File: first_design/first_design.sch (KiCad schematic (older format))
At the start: 57 parts

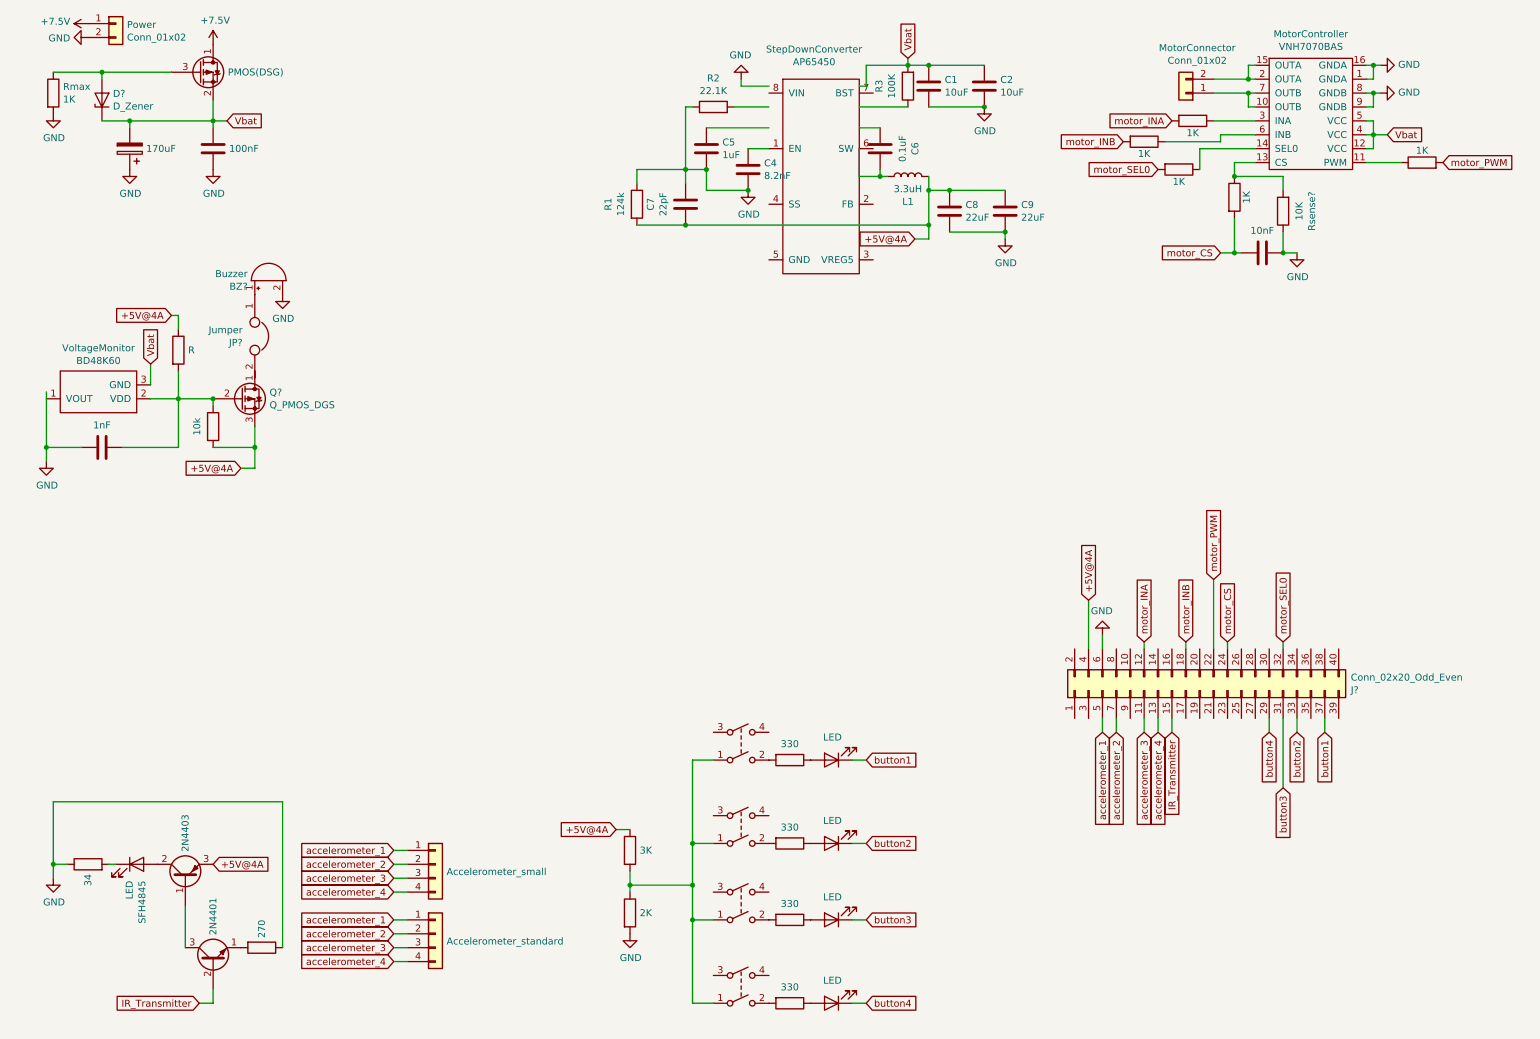
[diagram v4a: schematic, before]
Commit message: ldo added
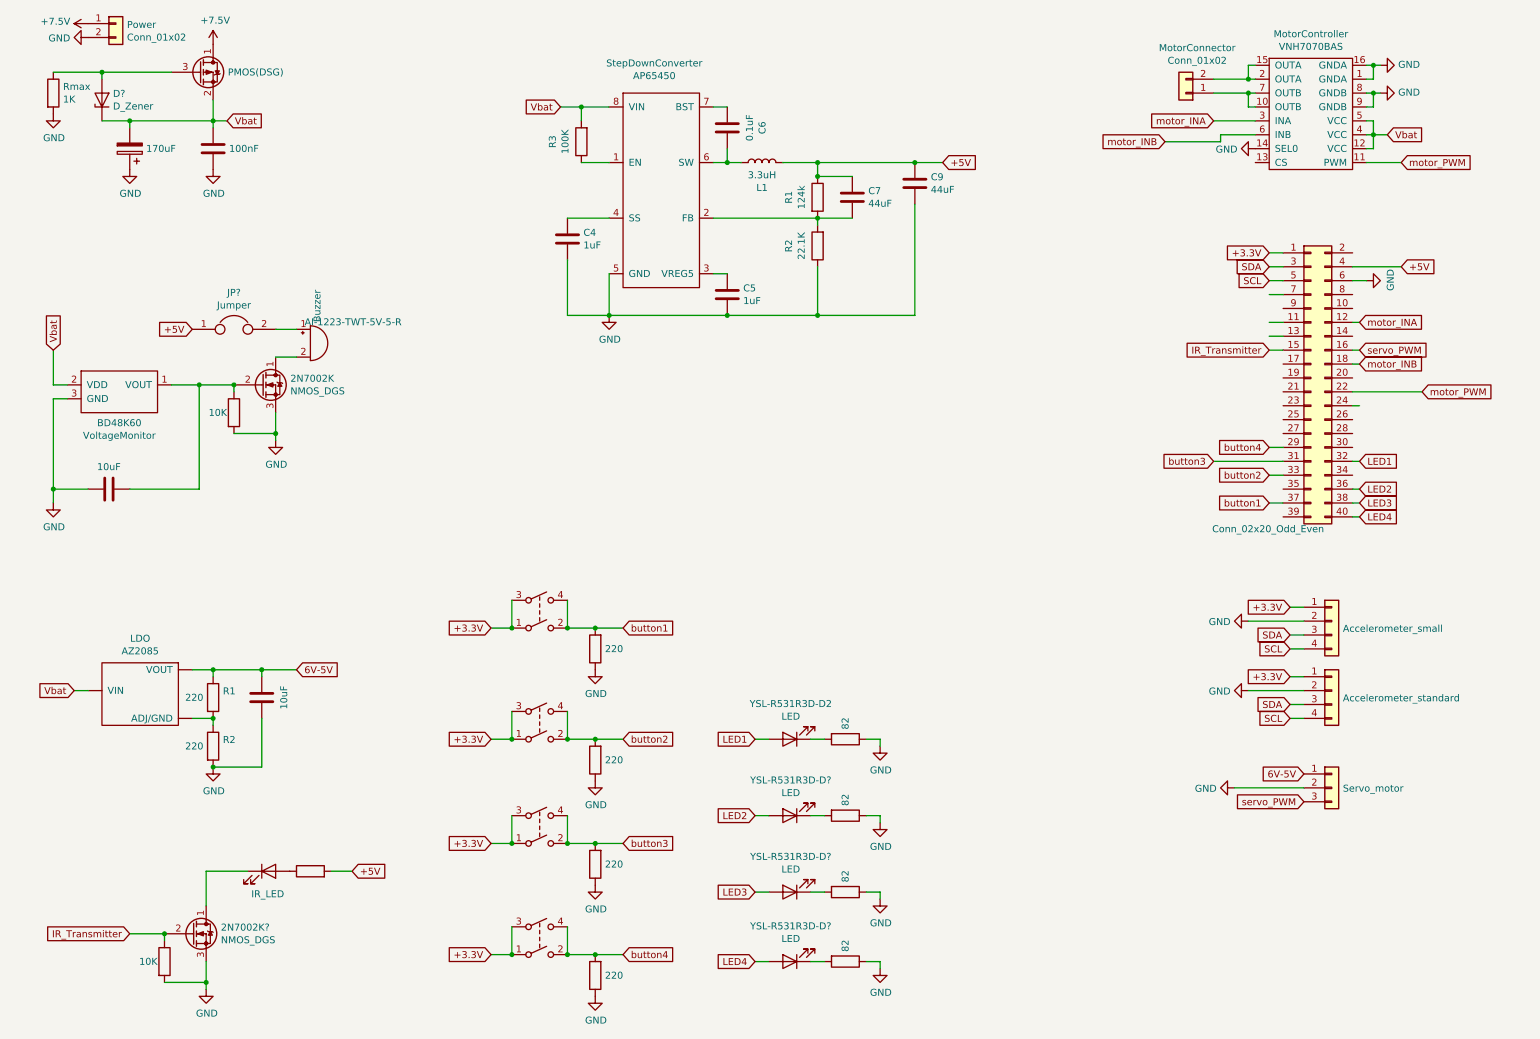
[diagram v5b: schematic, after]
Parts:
- removed 2N4401: BJT, symbol Transistor_BJT:2N2219
- removed C1, C2: 10uF, symbol Device:C
- removed C8: 22uF, symbol Device:C
- removed C?: 10nF, symbol Device:C
- removed D? (x3), SFH4845: LED, symbol Device:LED
- removed JP?: Jumper, symbol Device:Jumper
- removed Q?: Q_PMOS_DGS, symbol Device:Q_PMOS_DGS
- removed Q?: 2N4403, symbol Device:Q_PNP_BCE
- removed R? (x5): 1K, symbol Device:R
- removed R?: R, symbol Device:R
- removed R? (x4): 330, symbol Device:R
- removed R?: 3K, symbol Device:R
- removed R?: 2K, symbol Device:R
- removed R?: 34, symbol Device:R
- removed R?: 270, symbol Device:R
- removed Rsense?: 10K, symbol Device:R
- removed SW? (x4): SW_DPST, symbol Switch:SW_DPST
- added 2N7002K, 2N7002K?: NMOS_DGS, symbol Device:Q_NMOS_DGS
- added C?: 10uF, symbol Device:C
- added J?: Servo_motor, symbol Connector_Generic:Conn_01x03
- added JP?: Jumper, symbol Device:Jumper
- added LDO: AZ2085, symbol Converter_DCDC:AZ2085
- added None: IR_LED, symbol Device:LED
- added R1, R2, R? (x5): 220, symbol Device:R
- added R? (x4): 82, symbol Device:R
- added R?: 10K, symbol Device:R
- added SW? (x4): SW_DPST, symbol Switch:SW_DPST
- added YSL-R531R3D-D? (x3): LED, symbol Device:LED
- C4: value 8.2nF -> 1uF
- C7: value 22pF -> 44uF
- C9: value 22uF -> 44uF
- C?: value 1nF -> 10uF
- R?: value 10k -> 10K
- gave numbers to parts that had none: 2
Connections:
- net labels added: +3.3V, +5V, 6V-5V, LED1, LED2, LED3, LED4, SCL, SDA, servo_PWM
- net labels removed: +5V@4A, accelerometer_1, accelerometer_2, accelerometer_3, accelerometer_4, motor_CS, motor_SEL0
- wire segments 148 -> 163
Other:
- moved on the sheet: AI-1223-TWT-5V-5-R, C4, C5, C6, C9, L1, R1, R2, R3, StepDownConverter, VoltageMonitor

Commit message: footprint-libraries added
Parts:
- D1: renamed from D?; value D_Zener -> 5V
- Rmax1: renamed from Rmax; value 1K -> 280
- SPD30P06P_G1: renamed from Q?; value PMOS(DSG) -> PMOS
- gave numbers to parts that had none: 28
- renumbered AI-1223-TWT-5V-5-R to AI-1223-TWT-5V-5-R1, LDO to LDO1, MotorConnector to MotorConnector1, MotorController to MotorController1, None to None1, Power to Power1, R1 to R1_buck1, R2 to R2_buck1, StepDownConverter to StepDownConverter1, VoltageMonitor to VoltageMonitor1
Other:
- moved on the sheet: D1, Power1, Rmax1

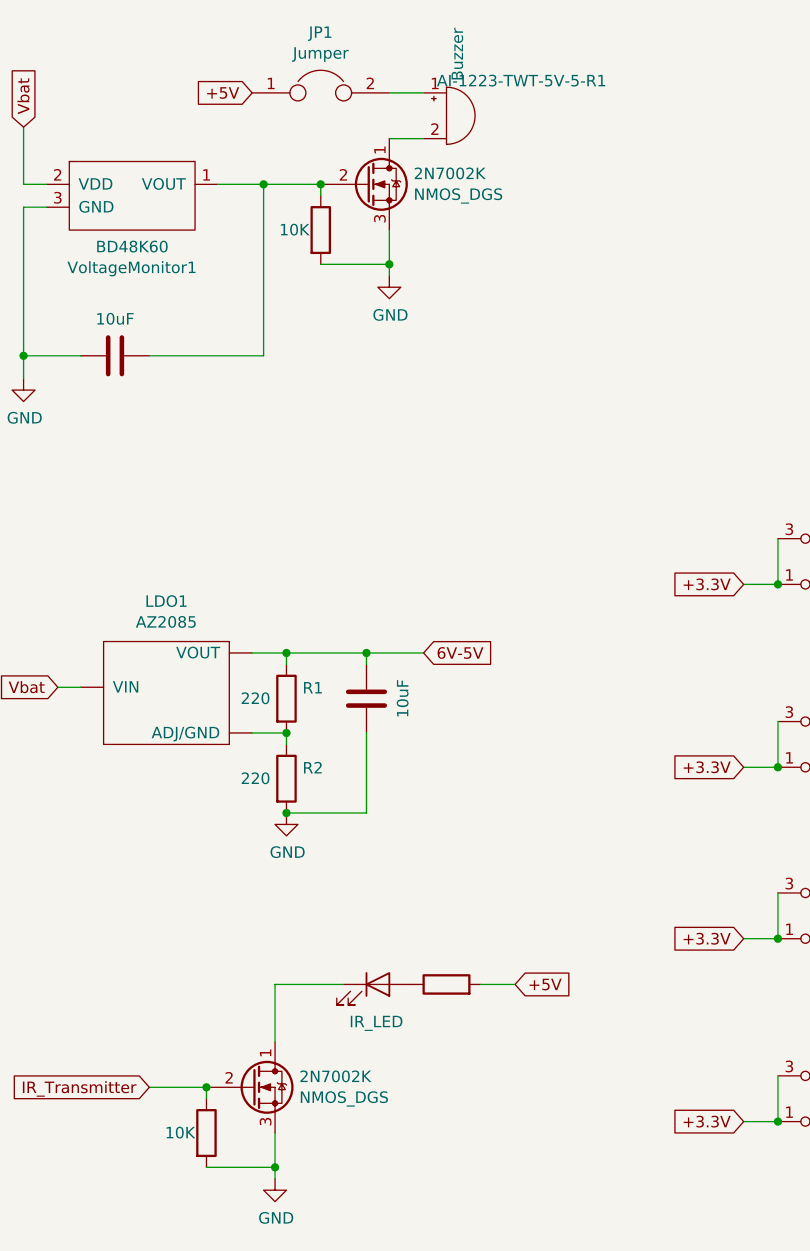
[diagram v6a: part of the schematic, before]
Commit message: updating footprints
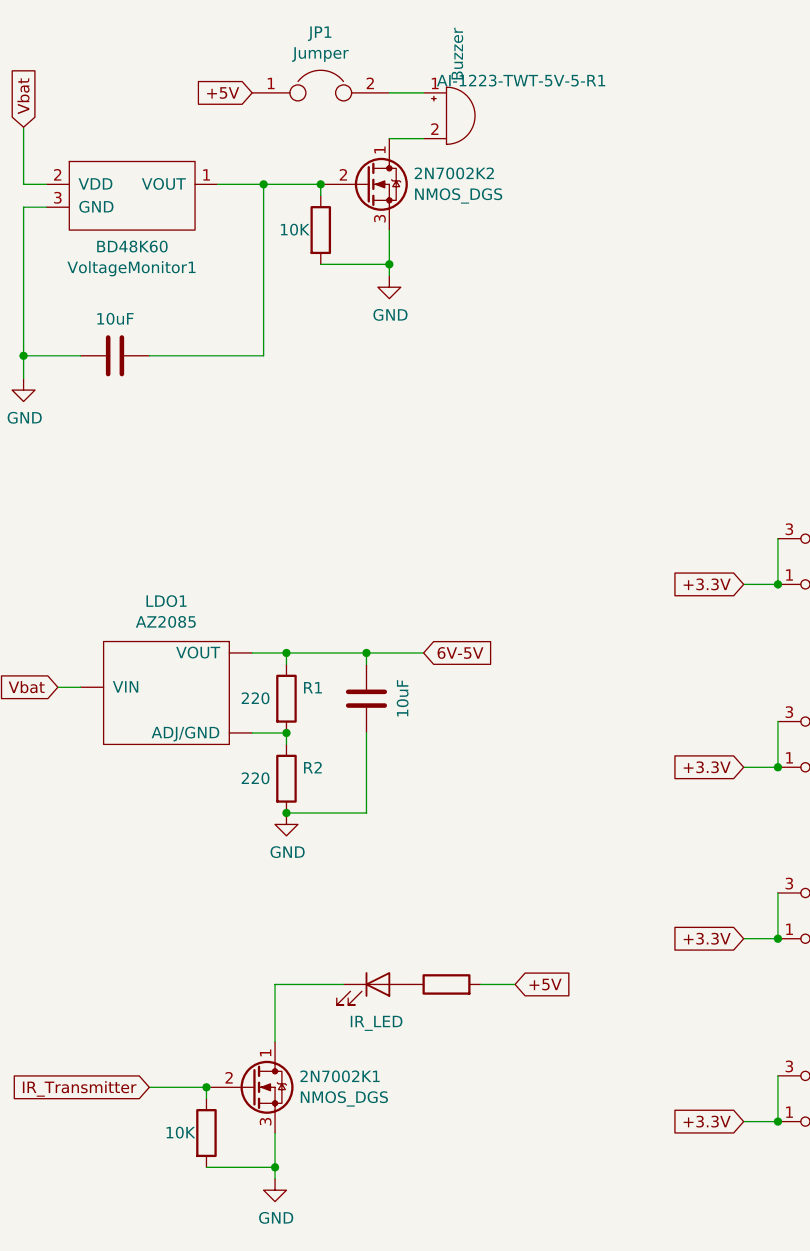
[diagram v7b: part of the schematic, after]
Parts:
- 2N7002K1, 2N7002K2: renamed from 2N7002K; footprint (none) -> Package_TO_SOT_SMD:SOT-23
- LDO1: footprint (none) -> Package_TO_SOT_SMD:TO-252-2
- StepDownConverter1: footprint (none) -> Package_SO:Diodes_SO-8EP
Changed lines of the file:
@@
 F 0 "StepDownConverter1" H 4925 1865 50  0000 C CNN
 F 1 "AP65450" H 4925 1774 50  0000 C CNN
-F 2 "" H 5350 1100 50  0001 C CNN
+F 2 "Package_SO:Diodes_SO-8EP" H 5350 1100 50  0001 C CNN
 F 3 "" H 5350 1100 50  0001 C CNN
 	1    4950 1350
@@
 	1900 3500 2200 3500
 $Comp
-L Device:Q_NMOS_DGS 2N7002K
+L Device:Q_NMOS_DGS 2N7002K2
 U 1 1 5D253C78
 P 2100 3150
-F 0 "2N7002K" H 2306 3196 50  0000 L CNN
+F 0 "2N7002K2" H 2306 3196 50  0000 L CNN
 F 1 "NMOS_DGS" H 2306 3105 50  0000 L CNN
-F 2 "" H 2300 3250 50  0001 C CNN
+F 2 "Package_TO_SOT_SMD:SOT-23" H 2300 3250 50  0001 C CNN
 F 3 "~" H 2100 3150 50  0001 C CNN
 	1    2100 3150
@@
 	1400 7450 1700 7450
 $Comp
-L Device:Q_NMOS_DGS 2N7002K
+L Device:Q_NMOS_DGS 2N7002K1
 U 1 1 5D7B4978
 P 1600 7100
-F 0 "2N7002K" H 1806 7146 50  0000 L CNN
+F 0 "2N7002K1" H 1806 7146 50  0000 L CNN
 F 1 "NMOS_DGS" H 1806 7055 50  0000 L CNN
-F 2 "" H 1800 7200 50  0001 C CNN
+F 2 "Package_TO_SOT_SMD:SOT-23" H 1800 7200 50  0001 C CNN
 F 3 "~" H 1600 7100 50  0001 C CNN
 	1    1600 7100
@@
 F 0 "LDO1" H 1225 5825 50  0000 C CNN
 F 1 "AZ2085" H 1225 5734 50  0000 C CNN
-F 2 "" H 1200 5100 50  0001 C CNN
+F 2 "Package_TO_SOT_SMD:TO-252-2" H 1200 5100 50  0001 C CNN
 F 3 "" H 1200 5100 50  0001 C CNN
 	1    1200 5400

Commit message: edge cut added
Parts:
- MotorController1: footprint (none) -> Package_SO:SOIC-16_3.9x9.9mm_P1.27mm
- SPD30P06P_G1: footprint (none) -> Package_TO_SOT_SMD:TO-252-2
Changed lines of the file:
@@
 F 0 "MotorController1" H 9650 1875 50  0000 C CNN
 F 1 "VNH7070BAS" H 9650 1784 50  0000 C CNN
-F 2 "" H 9650 850 50  0001 C CNN
+F 2 "Package_SO:SOIC-16_3.9x9.9mm_P1.27mm" H 9650 850 50  0001 C CNN
 F 3 "" H 9650 850 50  0001 C CNN
 	1    9650 1250
@@
 F 0 "SPD30P06P_G1" H 1906 1046 50  0000 L CNN
 F 1 "PMOS" H 1906 1000 50  0000 L CNN
-F 2 "" H 1900 1100 50  0001 C CNN
+F 2 "Package_TO_SOT_SMD:TO-252-2" H 1900 1100 50  0001 C CNN
 F 3 "~" H 1700 1000 50  0001 C CNN
 	1    1700 1000
